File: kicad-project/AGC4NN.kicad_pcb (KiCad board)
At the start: 2 copper layers, 20 x 12.5 mm, 13 parts, among them J1 Conn_01x04, Q1 MMBT3904, Q2 2N7002

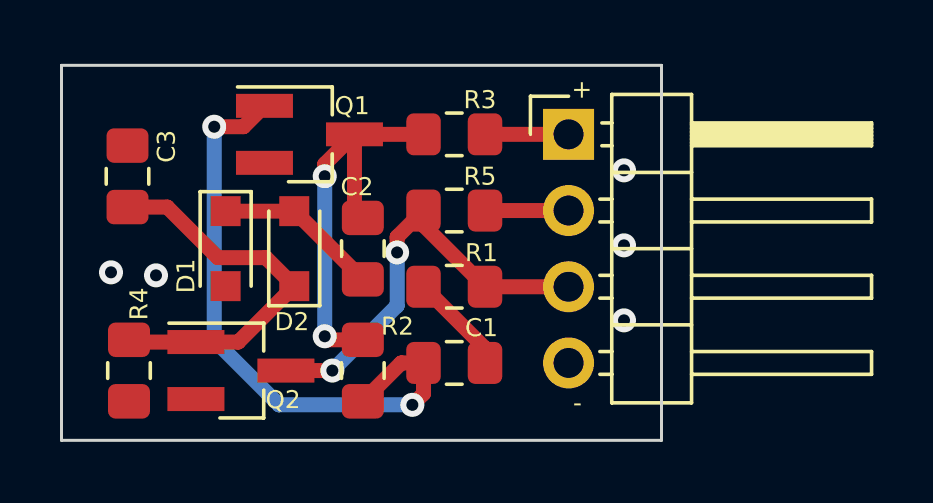
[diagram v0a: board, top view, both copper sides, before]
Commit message: Make a new PCB layout. Upgrade to v01.c.
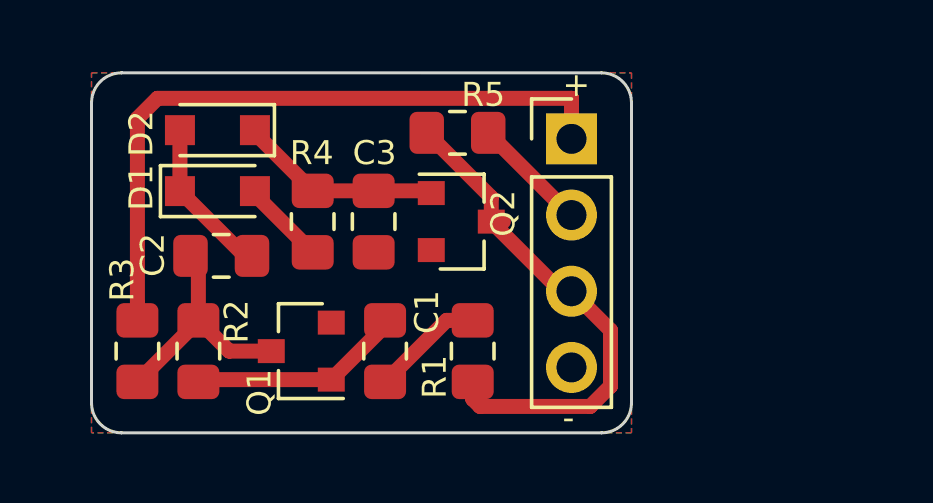
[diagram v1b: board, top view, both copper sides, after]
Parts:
- J1: footprint Connector_PinHeader_2.54mm:PinHeader_1x04_P2.54mm_Horizontal -> Connector_PinHeader_2.54mm:PinHeader_1x04_P2.54mm_Vertical
- Q1, Q2: footprint Package_TO_SOT_SMD:SOT-23_Handsoldering -> Package_TO_SOT_SMD:SOT-23
- moved R3 12.8 mm to (57.5, 49.3), turned to 270 degrees
- moved Q2 8.87 mm to (68.3, 45.0)
- moved C3 8.34 mm to (65.4, 45.0), turned to 270 degrees
- moved R4 7.88 mm to (63.4, 45.0)
- moved Q1 7.23 mm to (63.0, 49.3), turned to 180 degrees
- moved R2 5.52 mm to (59.6, 49.3)
- moved C2 4.73 mm to (60.3, 46.1), turned to 180 degrees
- moved D2 4.71 mm to (60.2, 41.9), turned to 180 degrees
- moved R5 2.59 mm to (68.2, 42.0)
- moved C1 2.34 mm to (65.8, 49.3), turned to 90 degrees
- moved R1 2.23 mm to (68.7, 49.3), turned to 270 degrees
- moved D1 1.94 mm to (60.2, 43.9), turned to 0 degrees
- moved J1 0.18 mm to (72.0, 42.2)
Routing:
- net VCC: track 2.78 -> 22.8 mm
- net Net-(C1-Pad2): track 20.7 -> 7.18 mm, vias 2 -> 0
- net Net-(C3-Pad1): track 13.3 -> 6.80 mm
- net Net-(C2-Pad2): track 13.7 -> 8.00 mm, vias 2 -> 0
- net GND: track 0.00 -> 2.84 mm, vias 5 -> 0
- net AF_OUT: track 14.4 -> 17.1 mm, vias 2 -> 0
- net AF_IN: track 2.78 -> 4.13 mm
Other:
- board size 20 x 12.5 mm -> 18 x 12 mm
- board text added: "BG1REN 20200101 AGC4NN v01.c, CQ11"
- board text removed: "BG1REN 20191231 AGC v01 / CQ11"
